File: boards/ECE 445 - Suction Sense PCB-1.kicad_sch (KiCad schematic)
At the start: 14 parts, among them U1 ESP32-WROOM-32E, U2 TPS2120YFPR, U3 AP62150Z6

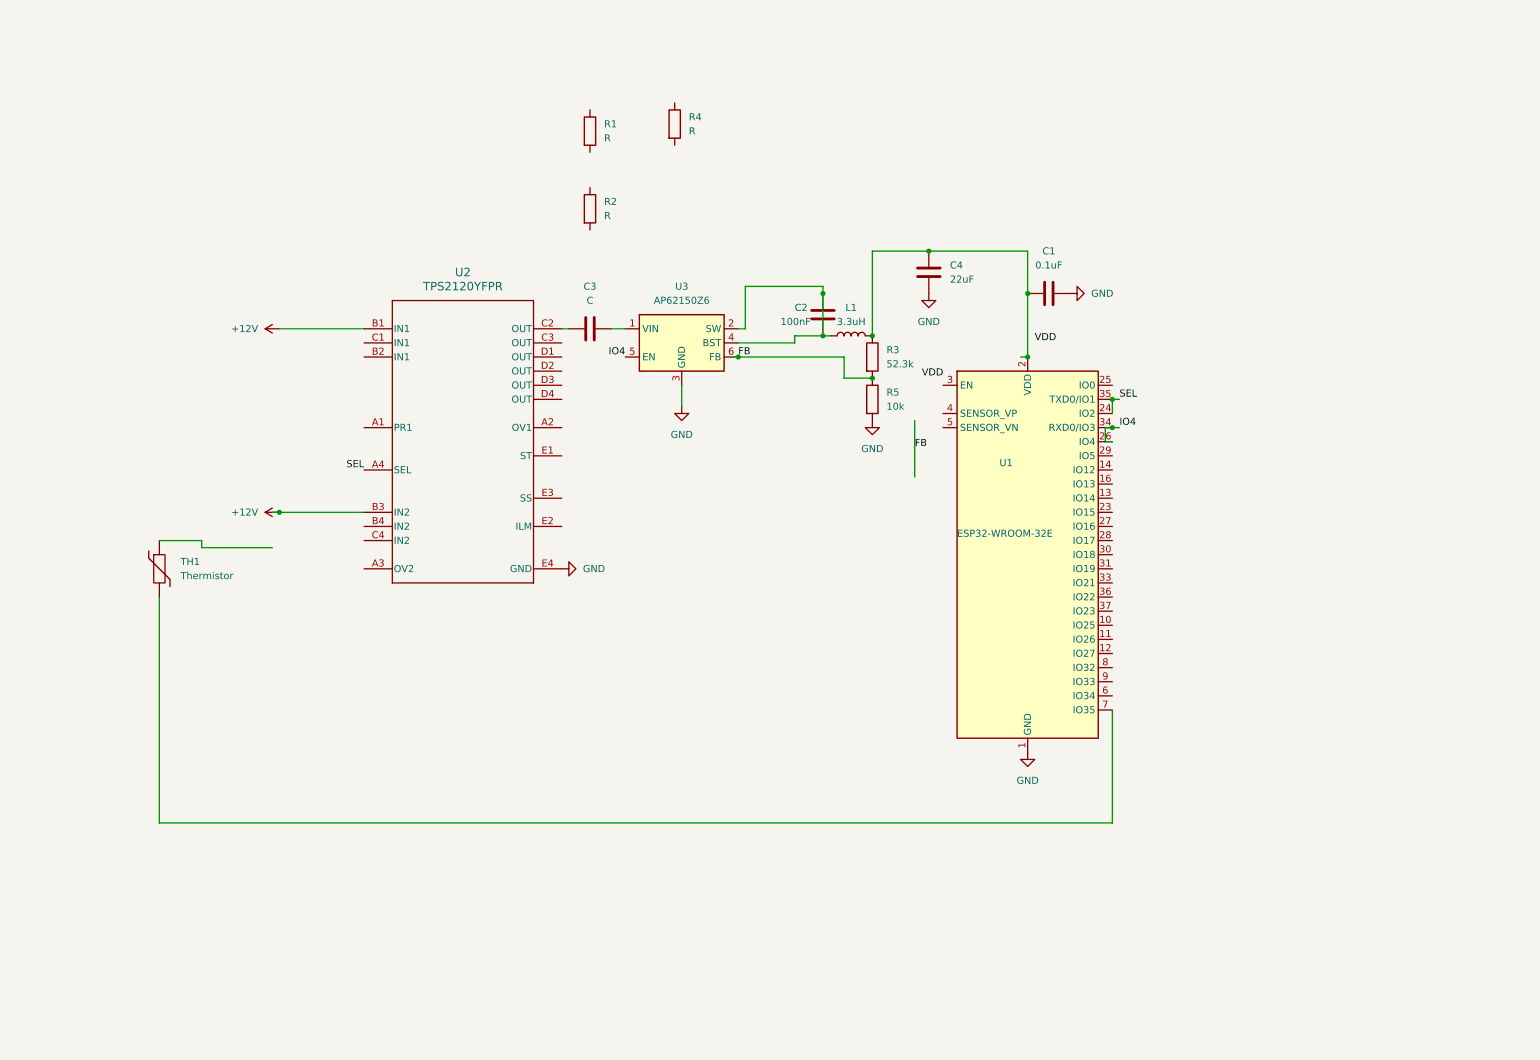
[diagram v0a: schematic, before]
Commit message: Finished PCB Schematic
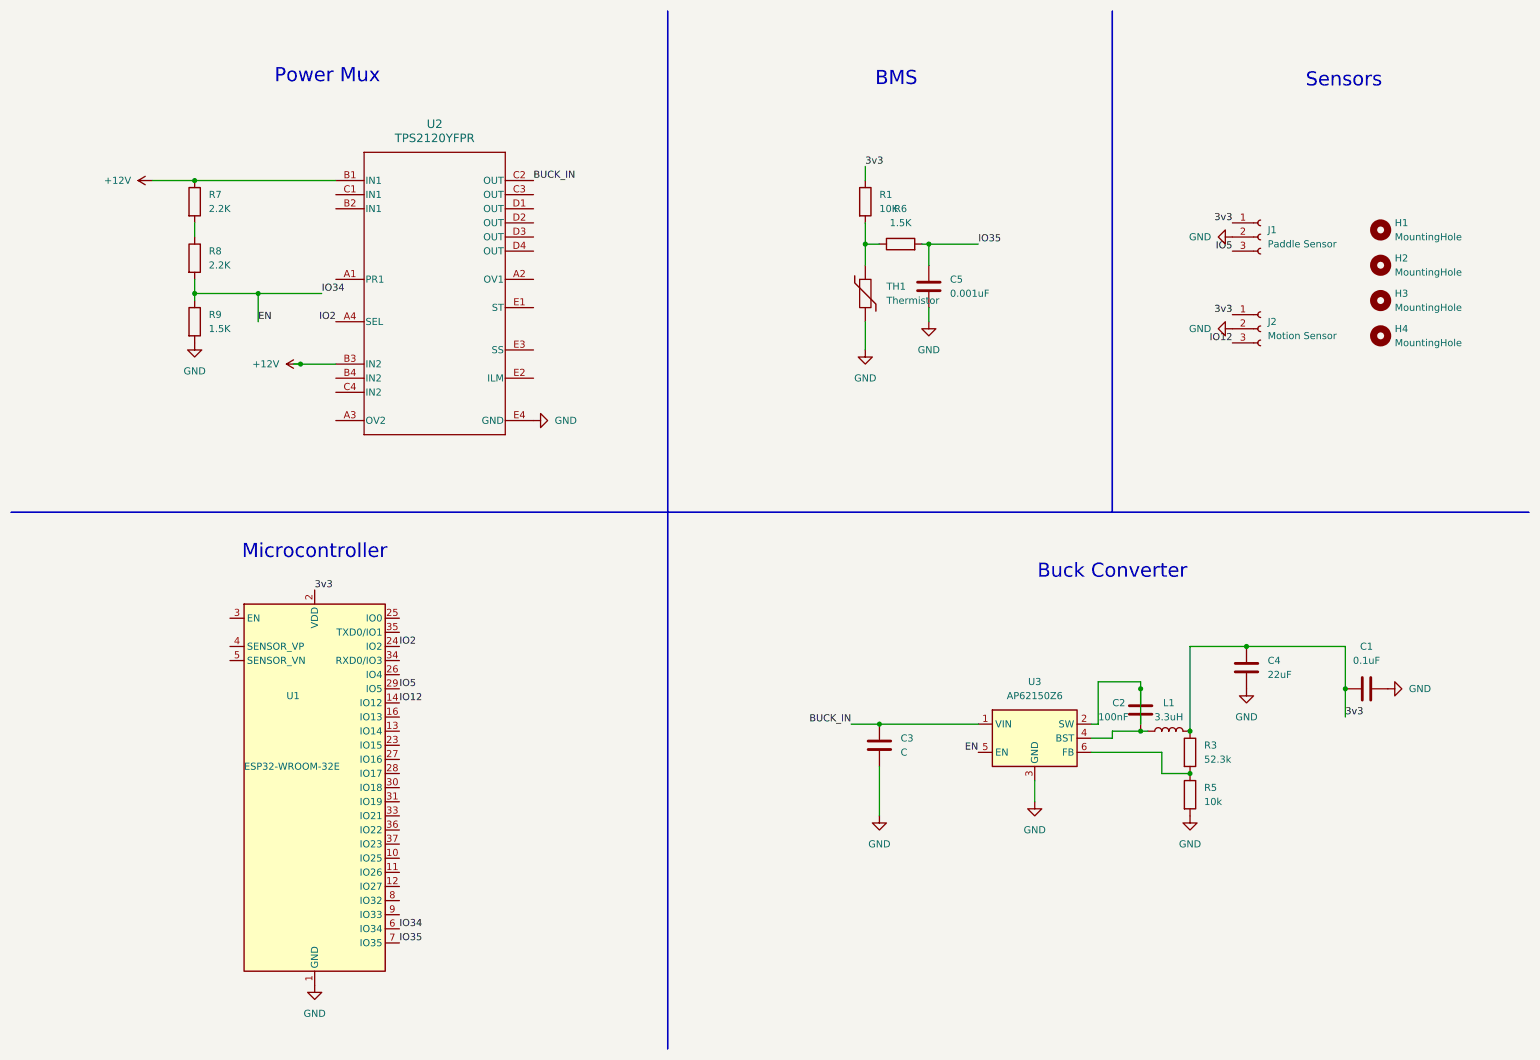
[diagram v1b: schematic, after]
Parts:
- removed R2, R4: R, symbol Device:R
- added C5: 0.001uF, symbol Device:C
- added H1, H2, H3, H4: MountingHole, symbol Mechanical:MountingHole
- added J1: Paddle Sensor, symbol Connector:Conn_01x03_Socket
- added J2: Motion Sensor, symbol Connector:Conn_01x03_Socket
- added R6, R9: 1.5K, symbol Device:R
- added R7, R8: 2.2K, symbol Device:R
- R1: value R -> 10K
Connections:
- net +12V: now also R7.1
- net GND: now also C3.2, TH1.2, C5.2, J1.2 (Pin_2), J2.2 (Pin_2), R9.2
- net 3v3: now reaches C1.1, C4.1, L1.2, R3.1, U1.2 (VDD)
- net 3v3: now also R1.1, J1.1 (Pin_1), J2.1 (Pin_1)
- net BUCK_IN: now reaches U3.1 (VIN)
- net BUCK_IN: now also C3.1, U2.C2 (OUT); no longer C3.2
- net at R1.2: now also TH1.1, R6.1
- net IO35: now reaches U1.7 (IO35)
- net IO35: now also C5.1, R6.2; no longer TH1.2
- net IO12: now reaches U1.14 (IO12)
- net IO12: now also J2.3 (Pin_3)
- net IO5: now reaches U1.29 (IO5)
- net IO5: now also J1.3 (Pin_3)
- net EN: now reaches U1.6 (IO34)
- net EN: now also U3.5 (EN), R8.2, R9.1
- net FB: no longer names the net of R3.2, R5.1, U3.6 (FB)
- removed net IO4: U1.26 (IO4), U1.34 (RXD0/IO3), U3.5 (EN)
- net SEL renamed IO2
- net IO2: no longer U1.35 (TXD0/IO1)
- new net: R7.2, R8.1
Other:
- note added: "BMS"
- note added: "Buck Converter"
- note added: "Microcontroller"
- note added: "Power Mux"
- note added: "Sensors"
- moved on the sheet: C1, C2, C3, C4, L1, R1, R3, R5, TH1, U1, U2, U3

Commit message: adding changes and updated pcb just needs routing
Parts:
- C1, C2, C3, C4, C5: footprint (none) -> Capacitor_SMD:CP_Elec_8x5.4
- H1, H2, H3, H4: footprint (none) -> MountingHole:MountingHole_3.2mm_M3
- J1, J2: footprint (none) -> Connector_Molex:Molex_KK-254_AE-6410-03A_1x03_P2.54mm_Vertical
- L1: footprint (none) -> Inductor_SMD:L_0805_2012Metric_Pad1.15x1.40mm_HandSolder
- R1, R3, R5, R6, R7, R8, R9, TH1: footprint (none) -> Resistor_SMD:R_0508_1220Metric
- U2: footprint YFP0020AAAA -> Library:YFP0020AAAA
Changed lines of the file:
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@@
 			)
 		)
-		(property "Footprint" ""
+		(property "Footprint" "MountingHole:MountingHole_3.2mm_M3"
 			(at 257.81 63.5 0)
 			(effects
@@
 			)
 		)
-		(property "Footprint" ""
+		(property "Footprint" "Capacitor_SMD:CP_Elec_8x5.4"
 			(at 177.4952 64.77 0)
 			(effects
@@
 			)
 		)
-		(property "Footprint" ""
+		(property "Footprint" "Inductor_SMD:L_0805_2012Metric_Pad1.15x1.40mm_HandSolder"
 			(at 219.71 140.97 0)
 			(effects
@@
 			)
 		)
-		(property "Footprint" ""
+		(property "Footprint" "MountingHole:MountingHole_3.2mm_M3"
 			(at 257.81 50.8 0)
 			(effects
@@
 			)
 		)
-		(property "Footprint" ""
+		(property "Footprint" "Resistor_SMD:R_0508_1220Metric"
 			(at 171.45 55.118 90)
 			(effects
@@
 			)
 		)
-		(property "Footprint" ""
+		(property "Footprint" "Connector_Molex:Molex_KK-254_AE-6410-03A_1x03_P2.54mm_Vertical"
 			(at 236.22 52.07 0)
 			(effects
@@
 			)
 		)
-		(property "Footprint" ""
+		(property "Footprint" "Capacitor_SMD:CP_Elec_8x5.4"
 			(at 215.5952 140.97 0)
 			(effects
@@
 			)
 		)
-		(property "Footprint" ""
+		(property "Footprint" "MountingHole:MountingHole_3.2mm_M3"
 			(at 257.81 57.15 0)
 			(effects
@@
 			)
 		)
-		(property "Footprint" ""
+		(property "Footprint" "Capacitor_SMD:CP_Elec_8x5.4"
 			(at 234.6452 133.35 0)
 			(effects
@@
 			)
 		)
-		(property "Footprint" ""
+		(property "Footprint" "Resistor_SMD:R_0508_1220Metric"
 			(at 163.322 45.72 90)
 			(effects
@@
 			)
 		)
-		(property "Footprint" ""
+		(property "Footprint" "Resistor_SMD:R_0508_1220Metric"
 			(at 221.742 152.4 90)
 			(effects
@@
 			)
 		)
-		(property "Footprint" ""
+		(property "Footprint" "Resistor_SMD:R_0508_1220Metric"
 			(at 165.1 62.23 0)
 			(effects
@@
 			)
 		)
-		(property "Footprint" ""
+		(property "Footprint" "Connector_Molex:Molex_KK-254_AE-6410-03A_1x03_P2.54mm_Vertical"
 			(at 236.22 68.58 0)
 			(effects
@@
 			)
 		)
-		(property "Footprint" ""
+		(property "Footprint" "Capacitor_SMD:CP_Elec_8x5.4"
 			(at 259.08 132.3848 0)
 			(effects
@@
 			)
 		)
-		(property "Footprint" ""
+		(property "Footprint" "Resistor_SMD:R_0508_1220Metric"
 			(at 221.742 144.78 90)
 			(effects
@@
 			)
 		)
-		(property "Footprint" ""
+		(property "Footprint" "Resistor_SMD:R_0508_1220Metric"
 			(at 42.672 67.31 90)
 			(effects
@@
 			)
 		)
-		(property "Footprint" ""
+		(property "Footprint" "Resistor_SMD:R_0508_1220Metric"
 			(at 42.672 45.72 90)
 			(effects
@@
 			)
 		)
-		(property "Footprint" ""
+		(property "Footprint" "Capacitor_SMD:CP_Elec_8x5.4"
 			(at 168.6052 147.32 0)
 			(effects
@@
 			)
 		)
-		(property "Footprint" "YFP0020AAAA"
+		(property "Footprint" "Library:YFP0020AAAA"
 			(at 87.63 62.23 0)
 			(effects
@@
 			)
 		)
-		(property "Footprint" ""
+		(property "Footprint" "MountingHole:MountingHole_3.2mm_M3"
 			(at 257.81 69.85 0)
 			(effects
@@
 			)
 		)
-		(property "Footprint" ""
+		(property "Footprint" "Resistor_SMD:R_0508_1220Metric"
 			(at 42.672 55.88 90)
 			(effects

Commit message: routed
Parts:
- added J3: Battery Connector, Connector_PinSocket_2.00mm:PinSocket_1x02_P2.00mm_Vertical, symbol Connector:Conn_01x02_Socket
- added J4: Barrel_Jack, Connector_BarrelJack:BarrelJack_CUI_PJ-036AH-SMT_Horizontal, symbol Connector:Barrel_Jack
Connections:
- net GND: now also J3.2 (Pin_2), J4.2
- net +12V renamed +12VA
- net +12VA: now also J3.1 (Pin_1); no longer U2.B3 (IN2)
- new net +12VB: J4.1, U2.B3 (IN2)
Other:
- note added: "+12VA"

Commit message: Changed voltage divider for powermux and also modified the buck converter Fb resistor network - Jeremy
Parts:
- removed R7: 2.2K, Resistor_SMD:R_0508_1220Metric, symbol Device:R
- added R2: 1.5K, Resistor_SMD:R_0508_1220Metric, symbol Device:R
- R3: value 52.3k -> 5.1K
- R5: value 10k -> 2.2K
- R8: value 2.2K -> 1.5K
- R9: value 1.5K -> 5.1K
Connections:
- net +12VA is gone; now on net +3.7VA: J3.1 (Pin_1), U2.B1 (IN1)
- net at R5.1, U3.6 (FB): now also R2.2; no longer R3.2
- net +3.7VA: now reaches R8.1
- net +12VB renamed +5VB
- new net: R2.1, R3.2
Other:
- note added: "+3.7VA"
- note removed: "+12VA"
- moved on the sheet: C2, L1, R3, R5

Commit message: finsih adding charging
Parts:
- added C6, C7: 4.7uF, Capacitor_SMD:C_0805_2012Metric_Pad1.18x1.45mm_HandSolder, symbol Device:C
- added D1, D2: LED_Small, LED_SMD:LED_0805_2012Metric, symbol Device:LED_Small
- added R10, R4: 850, Resistor_SMD:R_0805_2012Metric_Pad1.20x1.40mm_HandSolder, symbol Device:R
- added R7: 120k, Resistor_SMD:R_0805_2012Metric_Pad1.20x1.40mm_HandSolder, symbol Device:R
- added TP1: 3.7+, TestPoint:TestPoint_Pad_D2.0mm, symbol Connector:TestPoint
- added TP2: 3v3, TestPoint:TestPoint_Pad_D2.0mm, symbol Connector:TestPoint
- added TP3: BUCK_IN, TestPoint:TestPoint_Pad_D2.0mm, symbol Connector:TestPoint
- added U4: MCP73831-2-OT, Package_TO_SOT_SMD:SOT-23-5, symbol Battery_Management:MCP73831-2-OT
- C3: value C -> 440uf
- J3: footprint Connector_PinSocket_2.00mm:PinSocket_1x02_P2.00mm_Vertical -> Battery:BatteryHolder_Keystone_1057_1x2032
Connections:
- net +3.7VA: now also R4.2, TP1.1
- net +5VB: now also C6.2, R10.2, U4.4 (V_{DD})
- net 3v3: now also TP2.1
- net BUCK_IN: now also TP3.1
- net GND: now also C6.1, C7.2
- new net: R7.1, U4.5 (PROG)
- new net: R7.2, U4.2 (V_{SS})
- new net: D1.2 (A), R4.1
- new net: D2.1 (K), R10.1
- new net: D2.2 (A), U4.1 (STAT)
- new net 3.7+: C7.1, U4.3 (V_{BAT})

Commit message: adding changes to the journal and pcb design, as well as adding the LED gnd connection on schematic
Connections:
- net GND: now also D1.1 (K)
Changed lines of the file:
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@@
+	)
+	(symbol
+		(lib_id "power:GND")
+		(at 58.42 31.75 0)
+		(unit 1)
+		(exclude_from_sim no)
+		(in_bom yes)
+		(on_board yes)
+		(dnp no)
+		(fields_autoplaced yes)
+		(property "Reference" "#PWR019"
+			(at 58.42 38.1 0)
+			(effects
+				(font
+					(size 1.27 1.27)
+				)
+				(hide yes)
+			)
+		)
+		(property "Value" "GND"
+			(at 58.42 36.83 0)
+			(effects
+				(font
+					(size 1.27 1.27)
+				)
+			)
+		)
+		(property "Footprint" ""
+			(at 58.42 31.75 0)
+			(effects
+				(font
+					(size 1.27 1.27)
+				)
+				(hide yes)
+			)
+		)
+		(property "Datasheet" ""
+			(at 58.42 31.75 0)
+			(effects
+				(font
+					(size 1.27 1.27)
+				)
+				(hide yes)
+			)
+		)
+		(property "Description" "Power symbol creates a global label with name \"GND\" , ground"
+			(at 58.42 31.75 0)
+			(effects
+				(font
+					(size 1.27 1.27)
+				)
+				(hide yes)
+			)
+		)
+		(pin "1"
+		)
+		(instances
+			(project ""
+				(path "/561ea10a-797a-46d1-9f30-325f0302a4a7"
+					(reference "#PWR019")
+					(unit 1)
+				)
+			)
+		)
 	)
 	(symbol

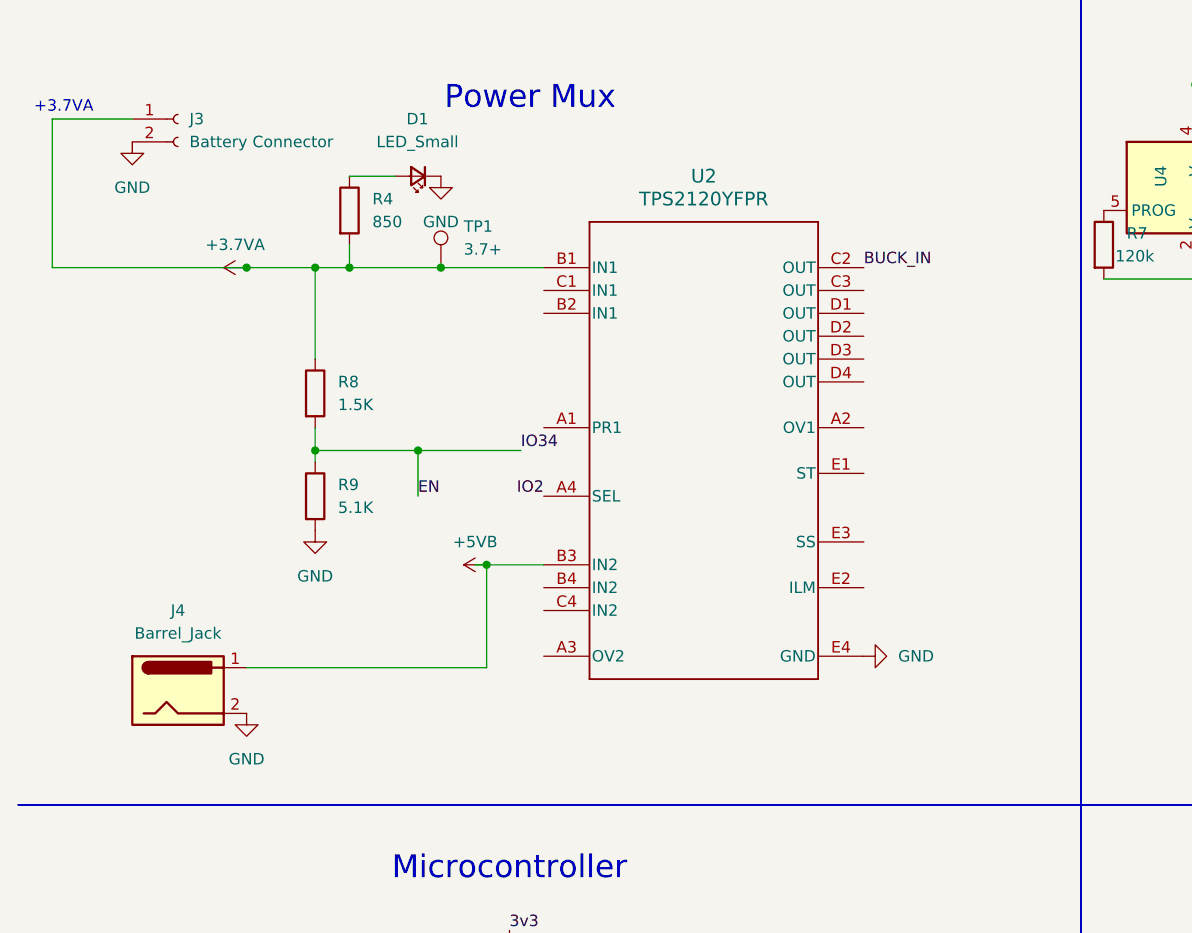
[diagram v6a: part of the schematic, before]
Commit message: routed with new footprint
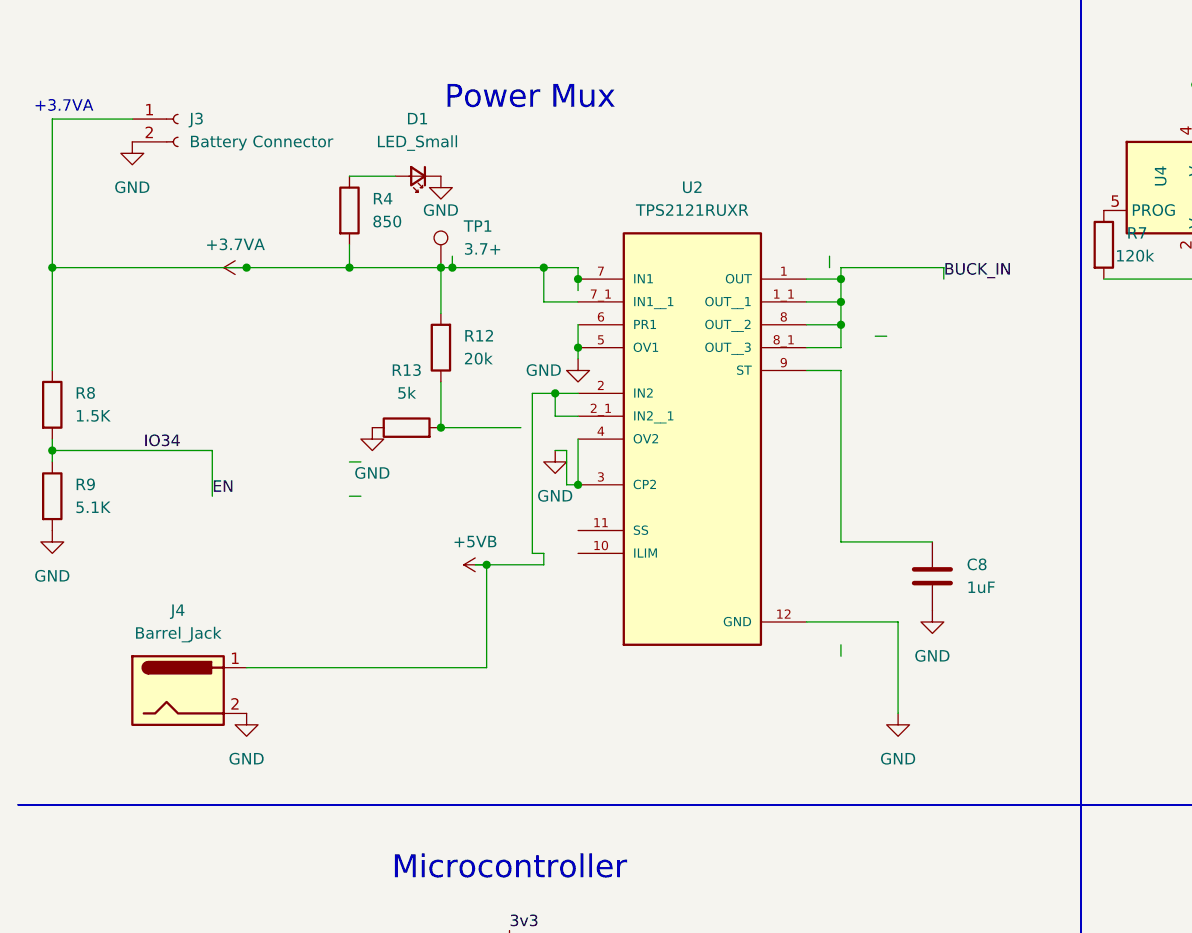
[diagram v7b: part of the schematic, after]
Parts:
- removed U2: TPS2120YFPR, Library:YFP0020AAAA, symbol 2025-09-26_00-52-33:TPS2120YFPR
- added C8: 1uF, Capacitor_SMD:C_0805_2012Metric_Pad1.18x1.45mm_HandSolder, symbol Device:C
- added R12: 20k, Resistor_SMD:R_0805_2012Metric_Pad1.20x1.40mm_HandSolder, symbol Device:R
- added R13: 5k, Resistor_SMD:R_0805_2012Metric_Pad1.20x1.40mm_HandSolder, symbol Device:R
- added U2: TPS2121RUXR, KiCadExtras:IC_TPS2121RUXR, symbol TPS2121RUXR:TPS2121RUXR
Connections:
- net +3.7VA: now also R12.2, U2.7 (IN1), U2.7_1 (IN1__1)
- net +5VB: now also U2.2 (IN2), U2.2_1 (IN2__1)
- net BUCK_IN: now also U2.1 (OUT), U2.1_1 (OUT__1), U2.8 (OUT__2), U2.8_1 (OUT__3)
- net GND: now also C8.2, R13.1, U2.12 (GND), U2.3 (CP2), U2.4 (OV2), U2.5 (OV1), U2.6 (PR1)
- new net: C8.1, U2.9 (ST)
- new net: R12.1, R13.2
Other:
- moved on the sheet: R8, R9
